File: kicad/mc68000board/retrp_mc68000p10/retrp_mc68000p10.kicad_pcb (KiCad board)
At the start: 4 copper layers, 95 x 65 mm, 13 parts, among them J1 Screw_Terminal_01x02, J2 Conn_02x32_Odd_Even, U1 68000D

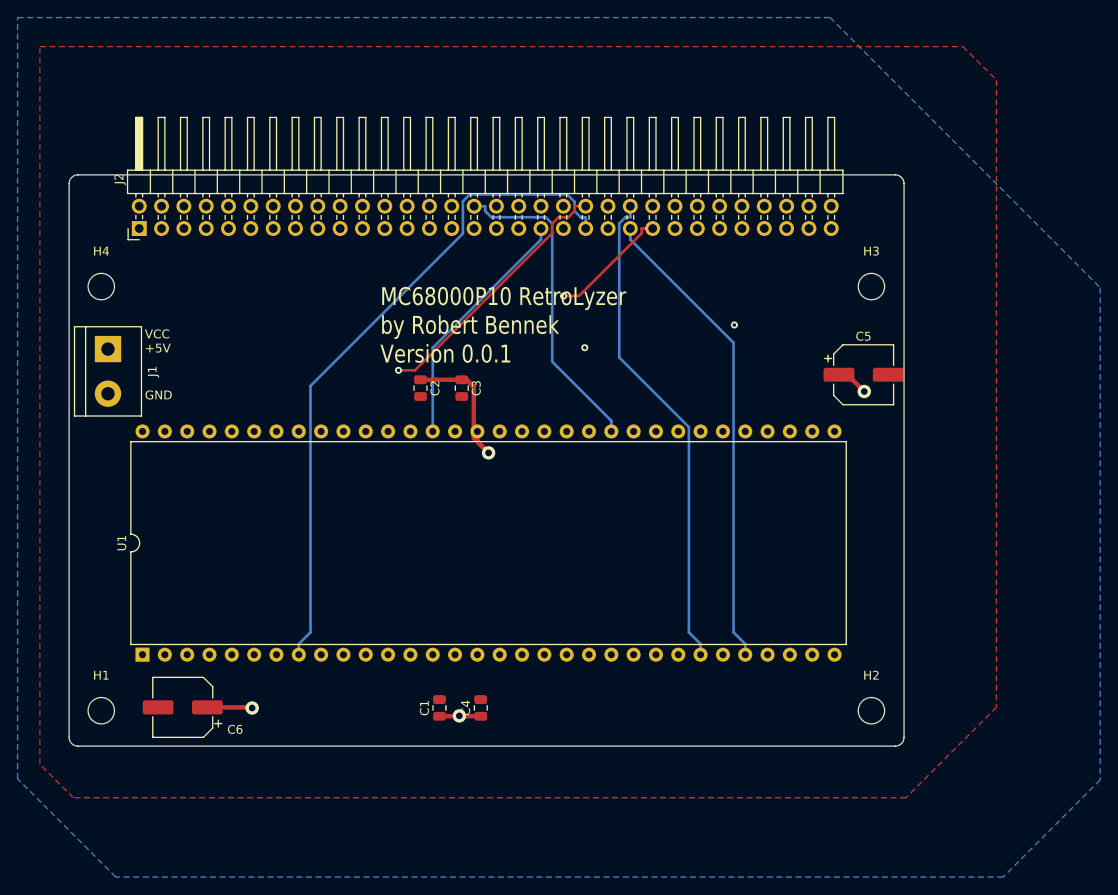
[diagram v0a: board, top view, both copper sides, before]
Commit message: #1 now with more on top & bottom layer
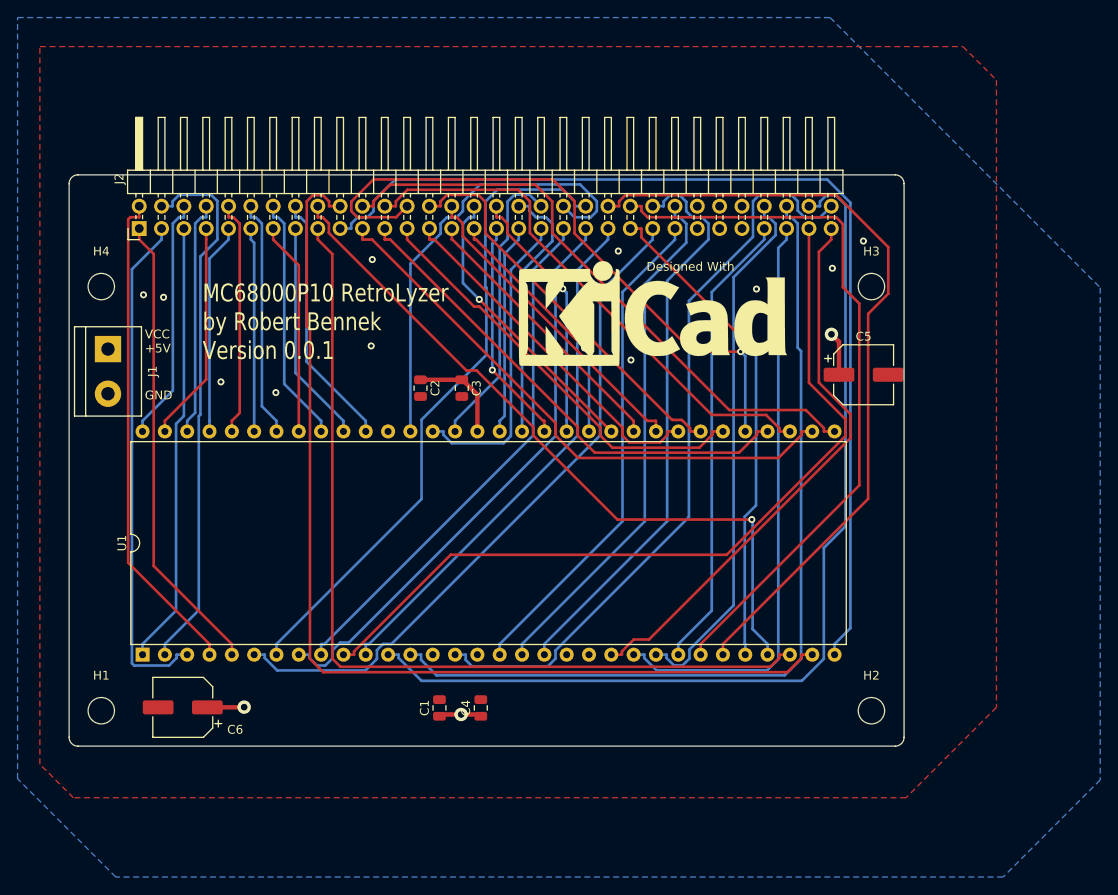
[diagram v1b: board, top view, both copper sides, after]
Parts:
- added REF**: KiCad-Logo_12mm_SilkScreen, Symbol:KiCad-Logo_12mm_SilkScreen, F.Cu at (136.4, 95.7)
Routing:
- net A4: track 77.8 -> 114.6 mm
- net A2: track 75.3 -> 102.9 mm
- net FC2: track 55.7 -> 82.6 mm
- net nBGACK: track 89.4 -> 110.2 mm
- net A9: track 53.3 -> 73.2 mm, vias 0 -> 1
- net A3: track 97.2 -> 116.0 mm
- net nDTACK: track 109.3 -> 93.0 mm
- net R/W: track 75.4 -> 60.1 mm
- net FC1: track 77.8 -> 89.3 mm
- net nLDS: track 76.6 -> 66.3 mm
- net IO_0: track 62.0 -> 52.9 mm
- net IO_3: track 52.5 -> 61.6 mm
- net CLK: track 78.6 -> 85.5 mm, vias 1 -> 0
- net A22: track 28.2 -> 35.0 mm
- net nUDS: track 68.1 -> 74.6 mm, vias 1 -> 0
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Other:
- board text added: "Designed With"

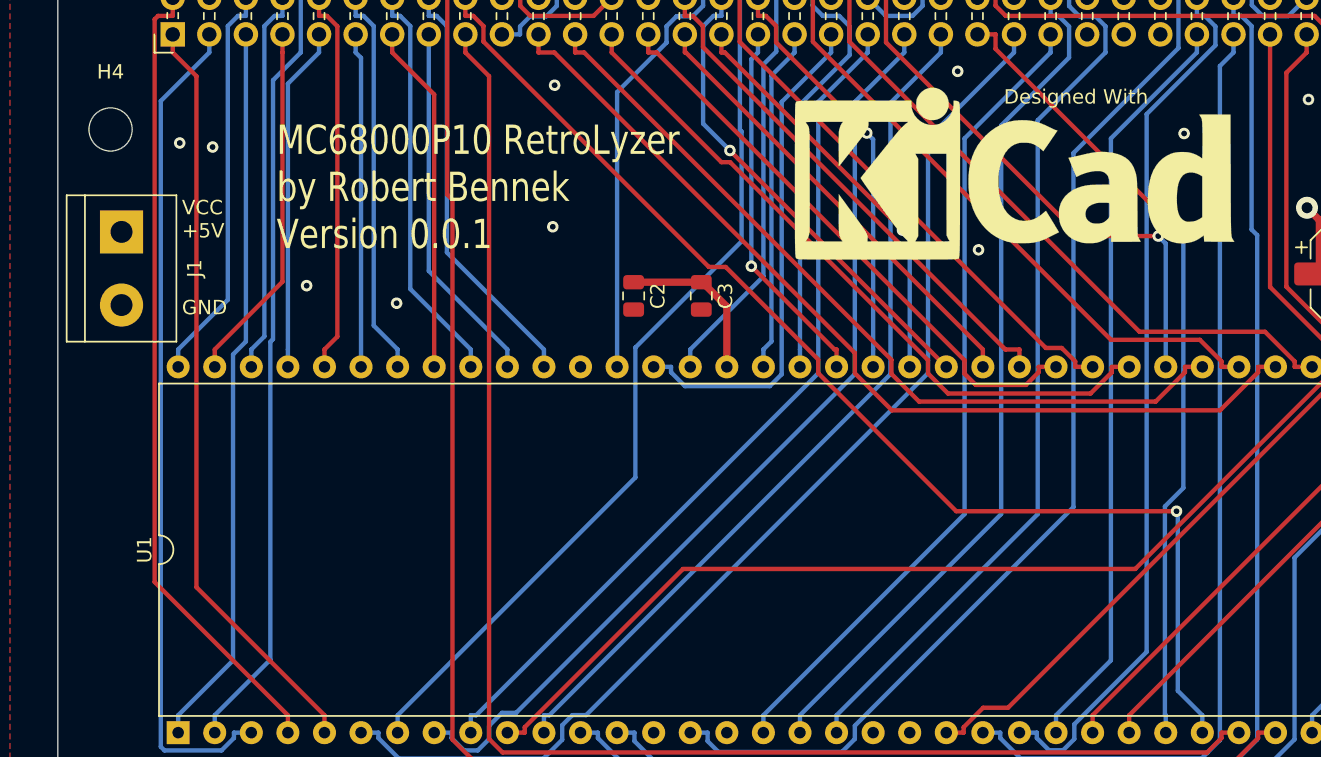
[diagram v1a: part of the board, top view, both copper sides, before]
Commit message: #1 now with rendered image
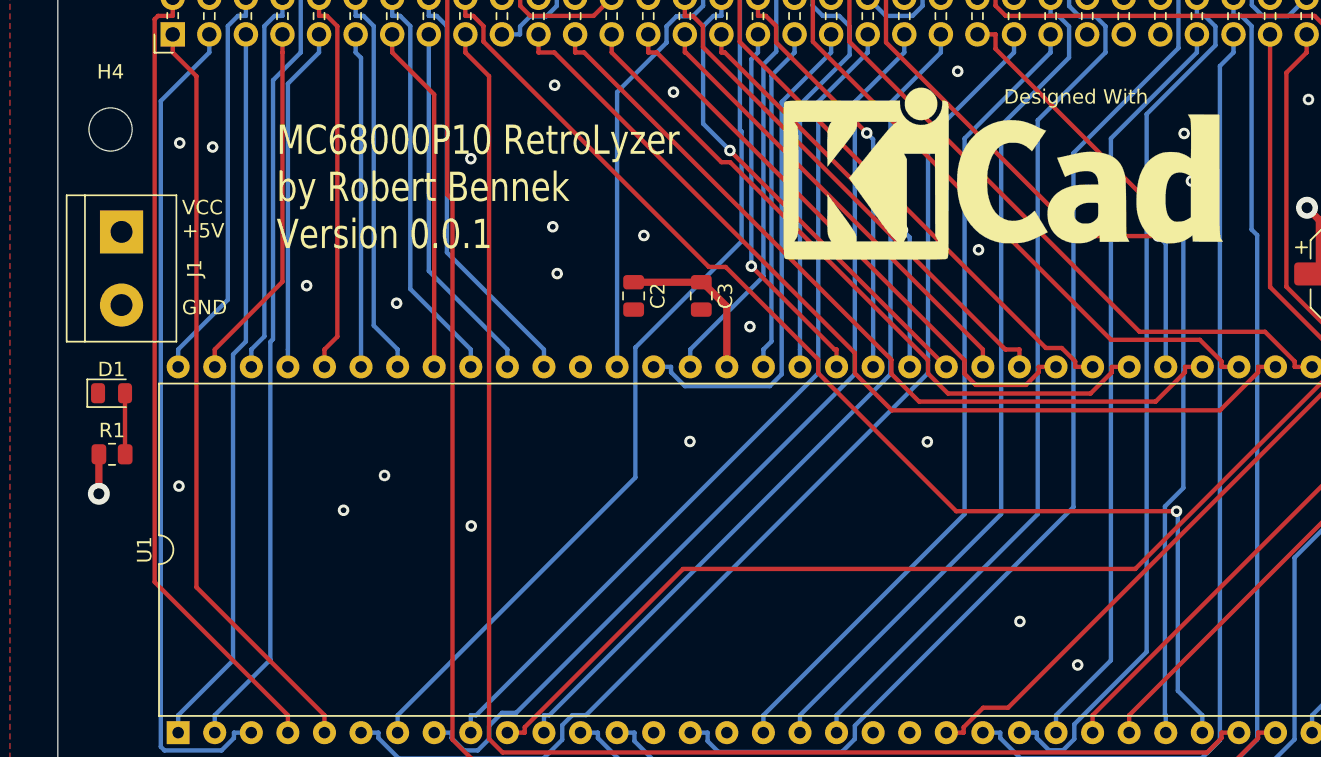
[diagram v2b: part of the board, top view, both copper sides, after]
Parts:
- added D1: Green, Diode_SMD:D_0805_2012Metric, F.Cu at (73.7, 111.0)
- added R1: 300, Resistor_SMD:R_0805_2012Metric, F.Cu at (73.8, 115.3)
- added REF**: KiCad-Logo_20mm_SilkScreen, Symbol:KiCad-Logo_20mm_SilkScreen, B.Cu at (117.7, 120.7)
- moved REF** 0.79 mm to (135.6, 95.7)
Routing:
- net Net-(D1-A): track 0.00 -> 4.24 mm
- net VCC: track 33.5 -> 36.3 mm, vias 3 -> 10
- net GND: vias 11 -> 19
